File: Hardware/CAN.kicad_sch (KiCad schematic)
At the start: 14 parts

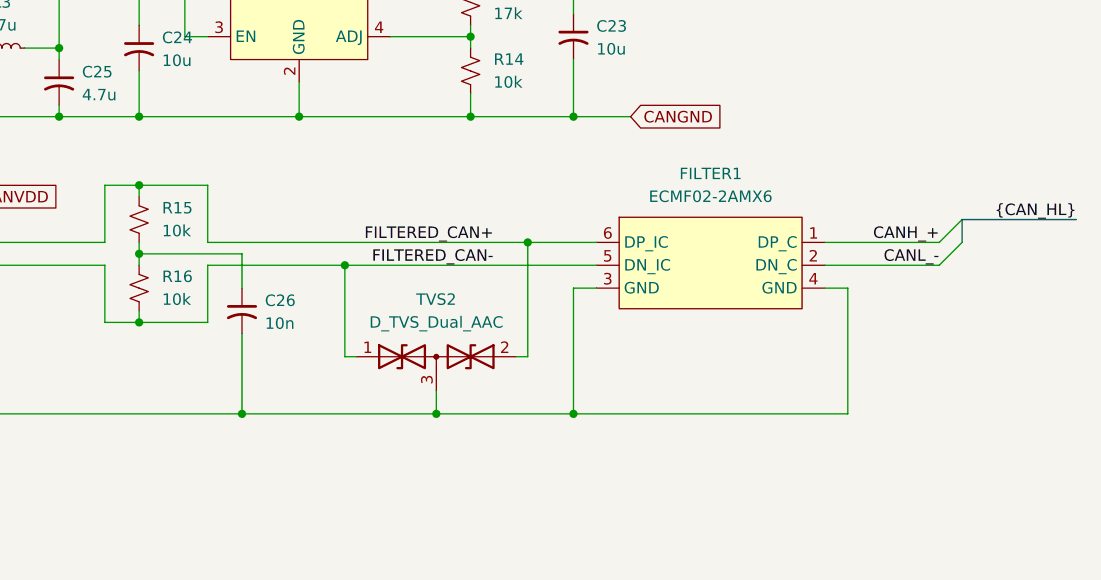
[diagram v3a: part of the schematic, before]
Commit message: Finished the board
- Board layout and routing is finished. Need to fix ~30 ERC errors and
  add thorough notes throughout, but otherwise that's it.
- Once ERC errors are resolved, will post BOM and Gerbers as a release.
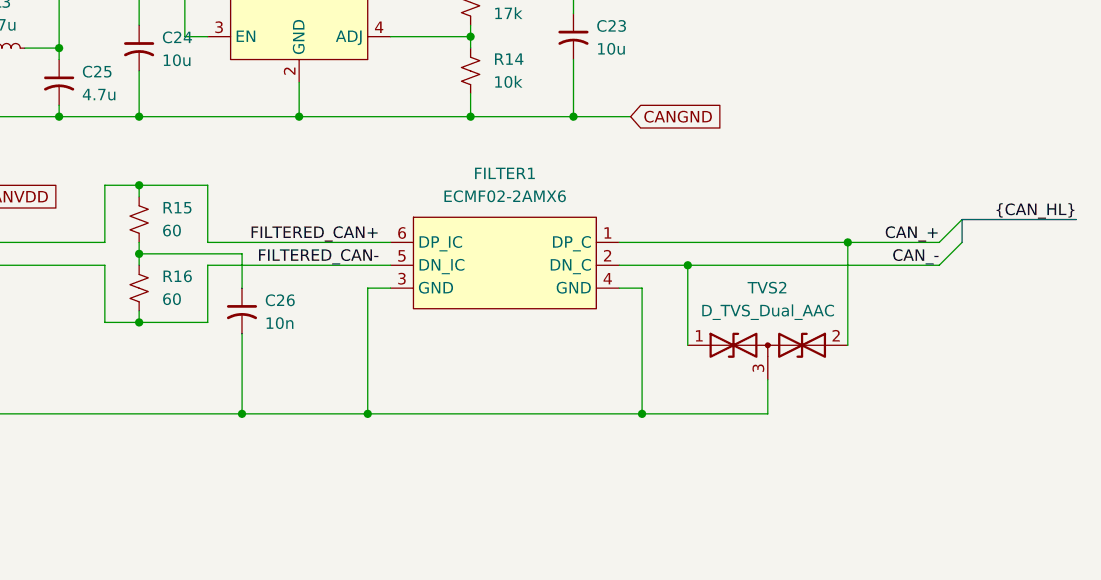
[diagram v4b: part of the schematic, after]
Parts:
- C23, C24, C26: footprint (none) -> Capacitor_SMD:C_0603_1608Metric_Pad1.08x0.95mm_HandSolder
- C25: footprint (none) -> Capacitor_SMD:CP_Elec_4x4.5
- CAN1: footprint (none) -> Package_SO:SOIC-16W_7.5x10.3mm_P1.27mm
- DCDC1: footprint (none) -> footprints:NME1S
- FILTER1: footprint (none) -> footprints:ECMF02-2AMX6_QFN-6L
- L3: footprint (none) -> Inductor_THT:L_Axial_L7.0mm_D3.3mm_P5.08mm_Vertical_Fastron_MICC
- LDO1: footprint (none) -> Package_TO_SOT_SMD:SOT-23-5_HandSoldering
- R13, R14: footprint (none) -> Resistor_SMD:R_0603_1608Metric_Pad0.98x0.95mm_HandSolder
- R15, R16: value 10k -> 60; footprint (none) -> Resistor_SMD:R_0603_1608Metric_Pad0.98x0.95mm_HandSolder
- TVS2: footprint (none) -> Package_TO_SOT_SMD:SOT-23
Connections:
- net FILTERED_CAN+: no longer TVS2.2 (A2)
- net FILTERED_CAN-: no longer TVS2.1 (A1)
- net at CAN1.4, CAN1.6, CAN1.7: now also CAN1.14
- net CANH_+ renamed CAN_+
- net CAN_+: now also TVS2.2 (A2)
- net CANL_- renamed CAN_-
- net CAN_-: now also TVS2.1 (A1)
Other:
- moved on the sheet: FILTER1, TVS2
